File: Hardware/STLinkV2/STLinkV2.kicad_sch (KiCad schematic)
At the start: 62 parts, among them J1 USB_B_Micro, J2 SWD, J3 ISP, J4 RS232, J5 JTAG, U1 STM32F103CBT6, U2 SRV05-4, U3 HT7833, U4 SRV05-4, U5 SRV05-4, U6 74AVCH2T45DC,125, U7 74AVCH2T45DC,125, Y1 8MHz

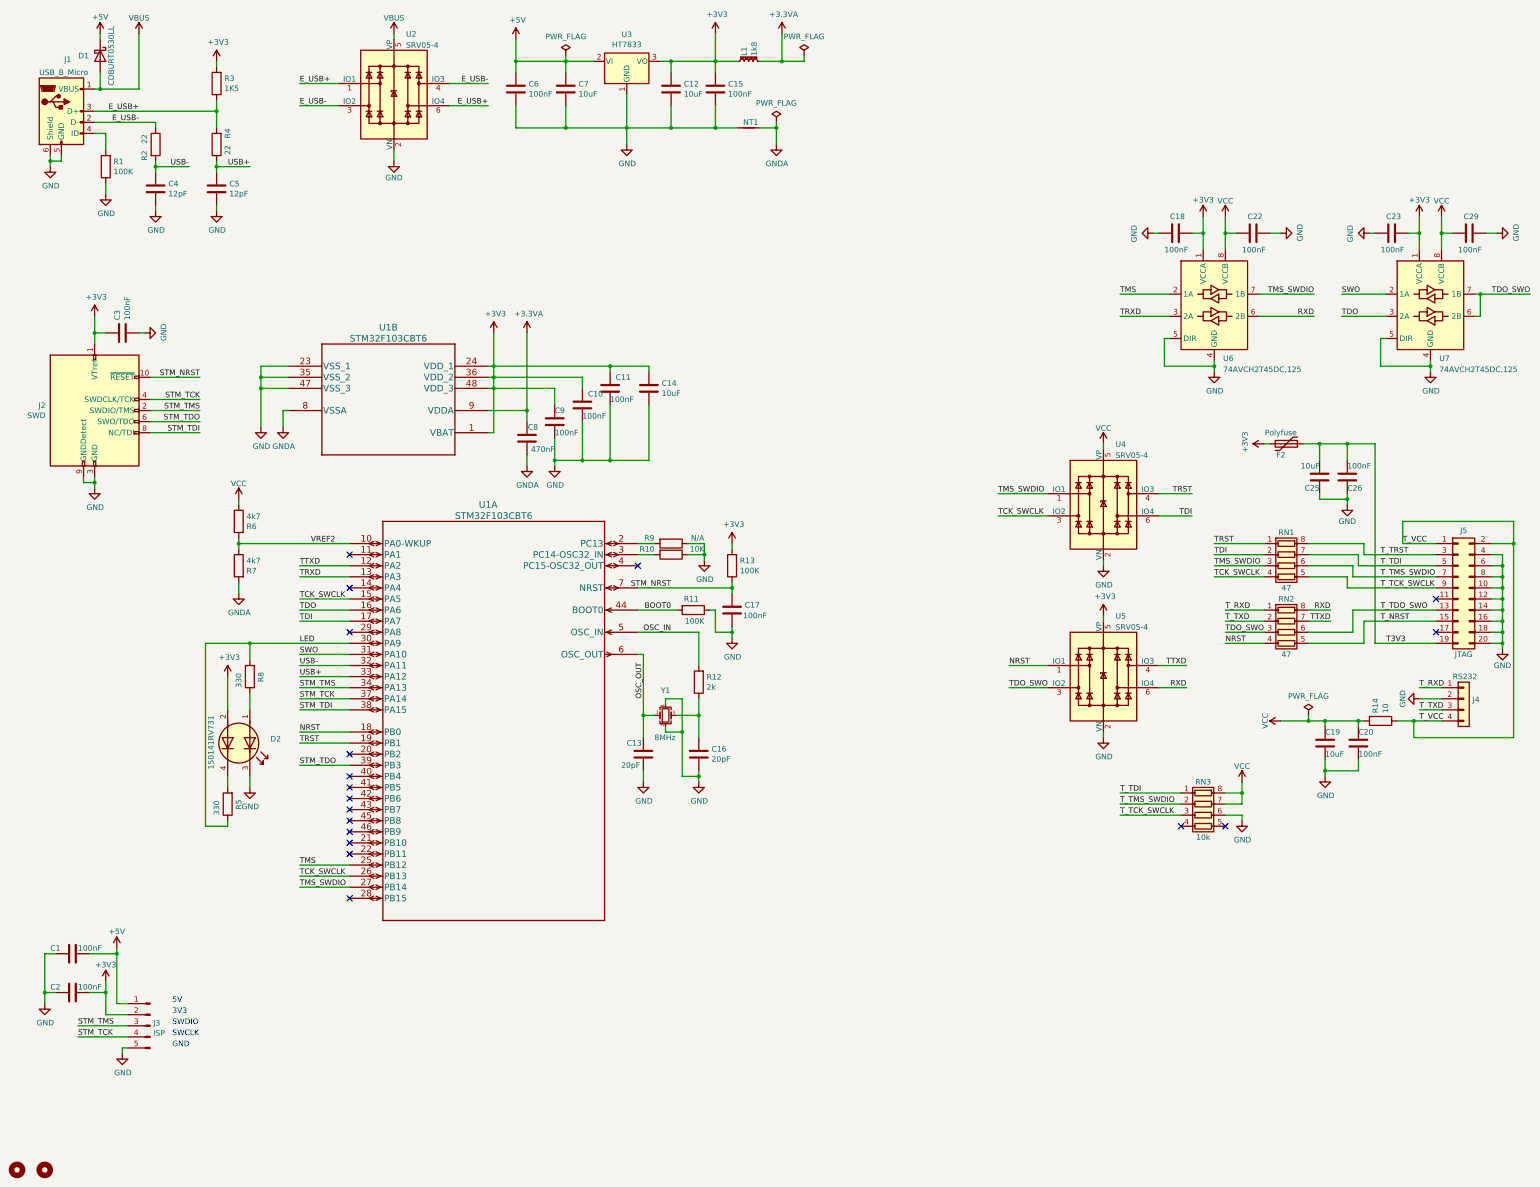
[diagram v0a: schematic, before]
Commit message: Minor fixes on the STLinkV2 board (no new version is required)
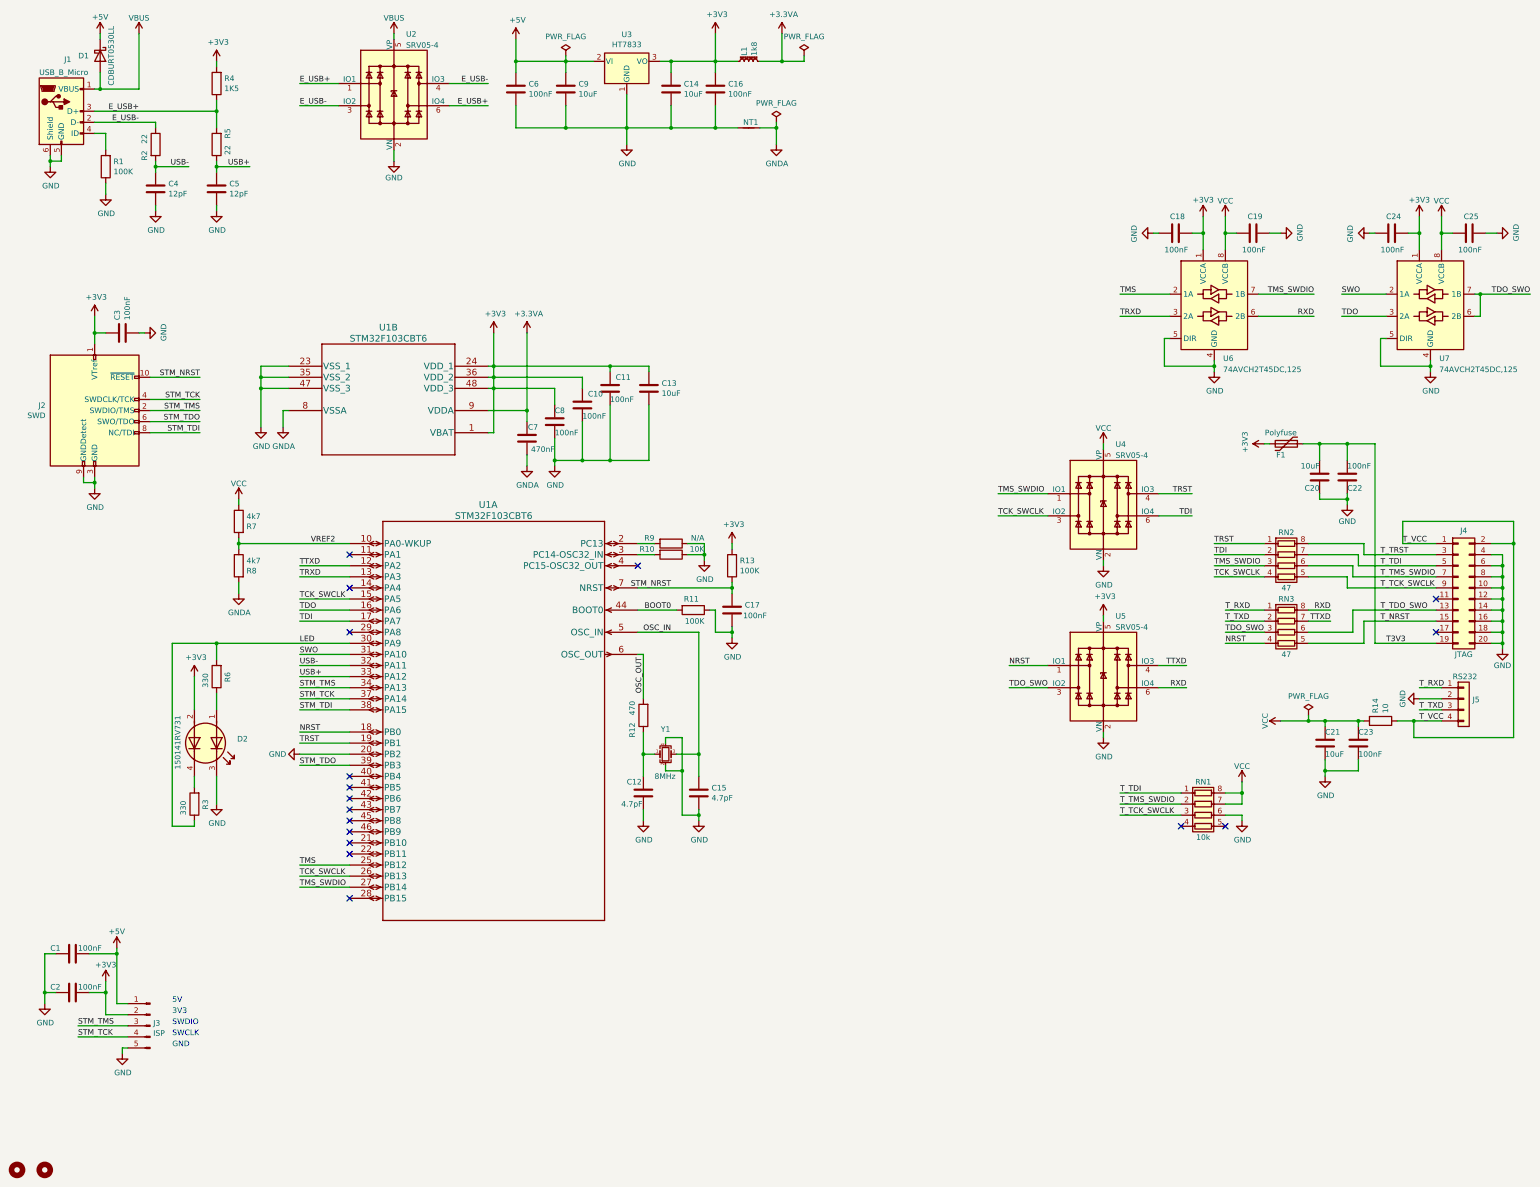
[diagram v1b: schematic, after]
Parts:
- C1, C10, C11, C17, C18, C2, C3, C6: LCSC C1525 -> (none)
- C12: renamed from C13; value 20pF -> 4.7pF; LCSC C1554 -> (none)
- C13: renamed from C14; LCSC C15525 -> (none)
- C15: renamed from C16; value 20pF -> 4.7pF; LCSC C1554 -> (none)
- C16: renamed from C15; LCSC C1525 -> (none)
- C19: renamed from C22; LCSC C1525 -> (none)
- C20: renamed from C25; LCSC C59461 -> (none)
- C21: renamed from C19; LCSC C15525 -> (none)
- C22: renamed from C26; LCSC C1525 -> (none)
- C23: renamed from C20; LCSC C1525 -> (none)
- C24: renamed from C23; LCSC C1525 -> (none)
- C25: renamed from C29; LCSC C1525 -> (none)
- C4, C5: LCSC C1554 -> (none)
- C7: renamed from C8; LCSC C47339 -> (none)
- C8: renamed from C9; LCSC C1525 -> (none)
- C9: renamed from C7; LCSC C19702 -> (none)
- D2: footprint LED_SMD:LED_Kingbright_AAA3528ESGCT -> LED_SMD:LED_RGB_Wuerth-PLCC4_3.2x2.8mm_150141M173100
- F1: renamed from F2; LSCS C207010 -> (none)
- J1: LCSC C91144 -> (none)
- R1, R11, R13, R14: LCSC C25741 -> (none)
- R12: value 2k -> 470; LCSC C4109 -> (none)
- R2: LCSC C25092 -> (none)
- R4: renamed from R3; LCSC C25867 -> (none)
- R5: renamed from R4; LCSC C25092 -> (none)
- R7: renamed from R6; LCSC C25900 -> (none)
- R8: renamed from R7; LCSC C25900 -> (none)
- U1: LCSC C8304 -> (none)
- renumbered C12 to C14, J5 to J4, J4 to J5, R5 to R3, R8 to R6, RN3 to RN1, RN1 to RN2, RN2 to RN3
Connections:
- net GND: now also U1.20 (PB2)
- net OSC_IN: now also C15.1, Y1.3; no longer R12.2
- net OSC_OUT: now also R12.2; no longer C12.1, Y1.1
- new net: C12.1, R12.1, Y1.1
- no-connect marks 18 -> 17
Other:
- moved on the sheet: C12, C15, D2, R12, R3, R6, Y1

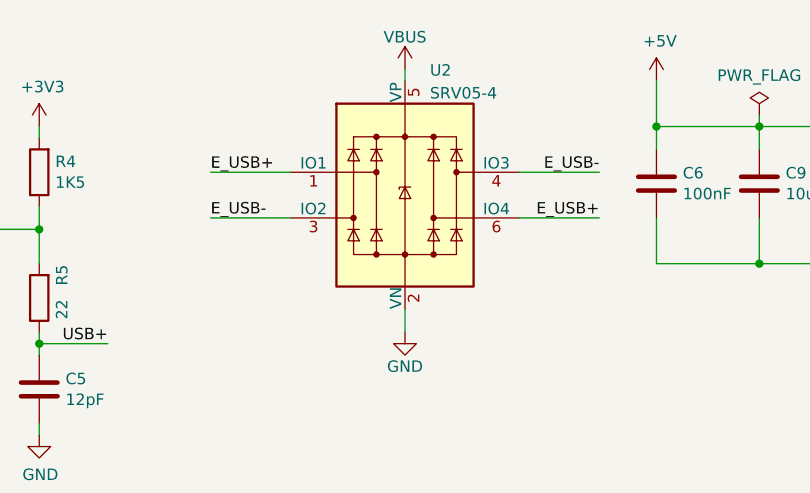
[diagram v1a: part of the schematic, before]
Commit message: Fixes on USB ESD protection
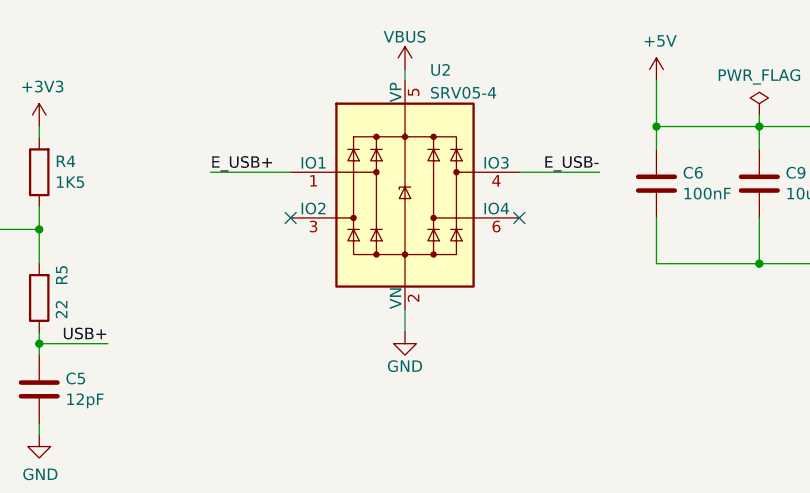
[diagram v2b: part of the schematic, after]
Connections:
- net E_USB+: no longer U2.6 (IO4)
- net E_USB-: no longer U2.3 (IO2)
- no-connect marks 17 -> 19
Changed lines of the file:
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@@
   (no_connect (at 91.44 190.5))
   (no_connect (at 91.44 203.2))
+  (no_connect (at 88.9 36.83))
   (no_connect (at 340.36 157.48))
   (no_connect (at 91.44 205.74))
@@
   (no_connect (at 157.48 142.24))
   (no_connect (at 91.44 198.12))
+  (no_connect (at 114.3 36.83))
   (no_connect (at 91.44 195.58))
   (no_connect (at 292.1 201.93))
@@
     (stroke (width 0) (type default) (color 0 0 0 0))
   )
-  (wire (pts (xy 80.01 36.83) (xy 88.9 36.83))
-    (stroke (width 0) (type default) (color 0 0 0 0))
-  )
   (wire (pts (xy 144.78 109.22) (xy 144.78 118.11))
     (stroke (width 0) (type default) (color 0 0 0 0))
@@
     (stroke (width 0) (type default) (color 0 0 0 0))
   )
-  (wire (pts (xy 114.3 36.83) (xy 123.19 36.83))
-    (stroke (width 0) (type default) (color 0 0 0 0))
-  )
   (wire (pts (xy 292.1 199.39) (xy 295.91 199.39))
     (stroke (width 0) (type default) (color 0 0 0 0))
@@
     (effects (font (size 1.27 1.27)) (justify left bottom))
   )
-  (label "E_USB-" (at 80.01 36.83 0)
-    (effects (font (size 1.27 1.27)) (justify left bottom))
-  )
   (label "STM_TDO" (at 57.15 109.22 180)
     (effects (font (size 1.27 1.27)) (justify right bottom))
@@
     (effects (font (size 1.27 1.27)) (justify right bottom))
   )
-  (label "E_USB+" (at 123.19 36.83 180)
-    (effects (font (size 1.27 1.27)) (justify right bottom))
-  )

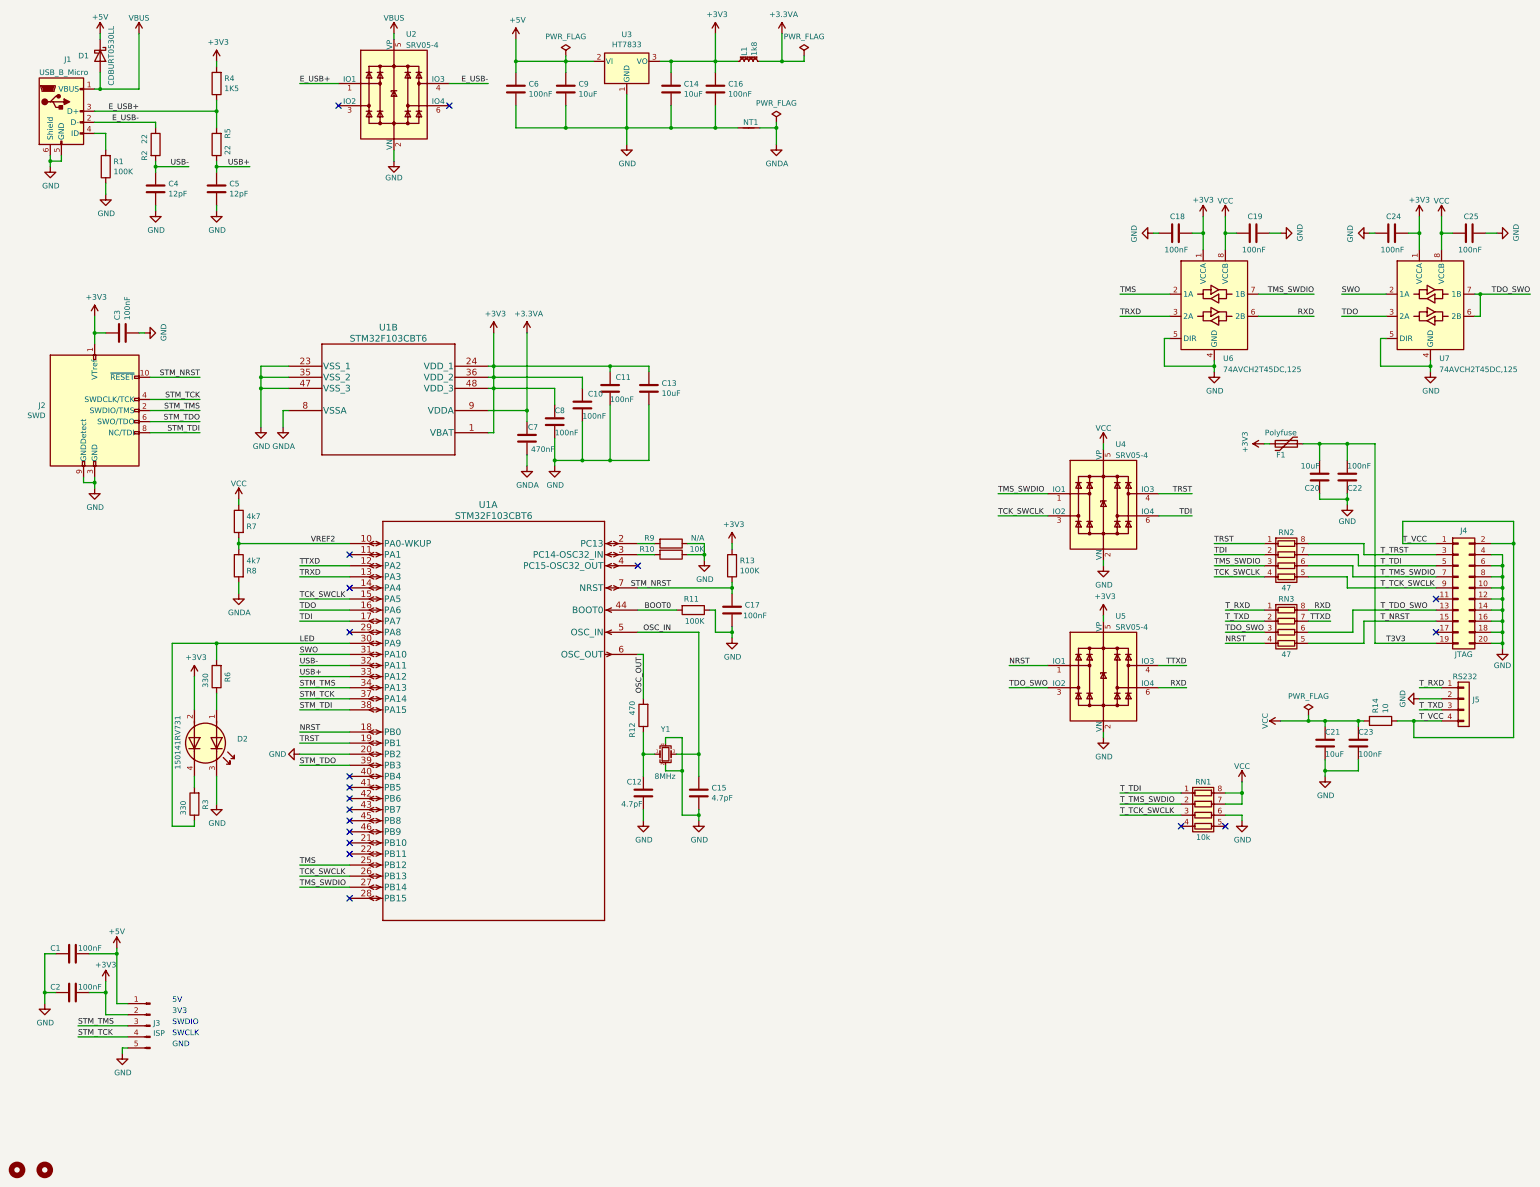
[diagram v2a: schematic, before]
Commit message: Relabeled SWD lines on STLinkV2 schematics, since they were misleading.
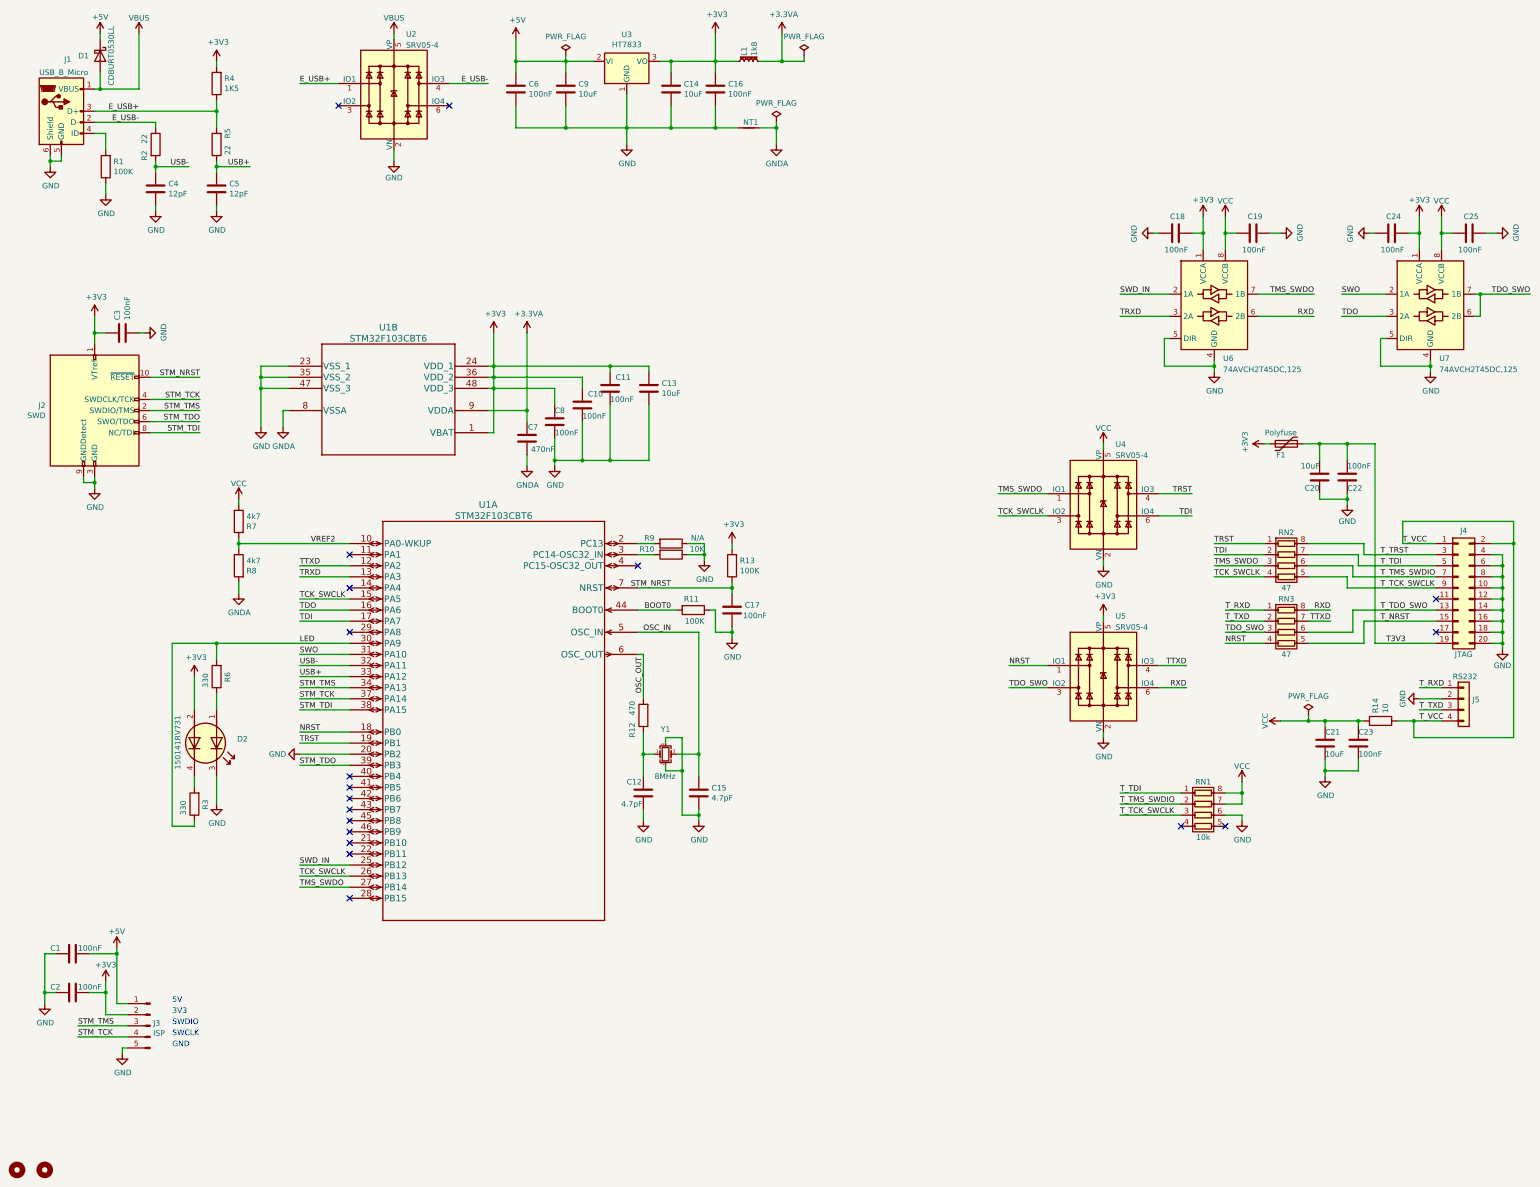
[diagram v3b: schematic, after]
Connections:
- net TMS renamed SWD_IN
- net TMS_SWDIO renamed TMS_SWDO
